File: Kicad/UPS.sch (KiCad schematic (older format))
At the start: 6 parts, among them J1 Raspberry_Pi_2_3, U1 CW2015

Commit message: Placing component
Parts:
- added D? (x4): LED, symbol Device:LED
- added SW?: SW_Push, symbol Switch:SW_Push
- added U?: ip5306, symbol ip5306:ip5306
- added U?: ETA1096, symbol eta1096:ETA1096
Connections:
- wire segments 20 -> 37
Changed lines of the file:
@@
 Text Label 6400 3650 0    50   ~ 0
 GND
+Wire Notes Line
+	750  1150 1300 1150
+Wire Notes Line
+	1300 1150 1300 2850
+Wire Notes Line
+	1300 2850 750  2850
+Wire Notes Line
+	750  2850 750  1150
+$Comp
+L eta1096:ETA1096 U?
+U 1 1 5D5AC856
+P 4000 4200
+F 0 "U?" H 3950 4225 50  0000 C CNN
+F 1 "ETA1096" H 3950 4134 50  0000 C CNN
+F 2 "" V 4350 3900 50  0001 C CNN
+F 3 "" V 4350 3900 50  0001 C CNN
+	1    4000 4200
+	1    0    0    -1
+$EndComp
+$Comp
+L ip5306:ip5306 U?
+U 1 1 5D5AA443
+P 4000 3150
+F 0 "U?" H 3950 3175 50  0000 C CNN
+F 1 "ip5306" H 3950 3084 50  0000 C CNN
+F 2 "" V 4350 2850 50  0001 C CNN
+F 3 "" V 4350 2850 50  0001 C CNN
+	1    4000 3150
+	1    0    0    -1
+$EndComp
+$Comp
+L Device:LED D?
+U 1 1 5D5ABF8A
+P 1900 3800
+F 0 "D?" V 1847 3878 50  0000 L CNN
+F 1 "LED" V 1938 3878 50  0000 L CNN
+F 2 "" H 1900 3800 50  0001 C CNN
+F 3 "~" H 1900 3800 50  0001 C CNN
+	1    1900 3800
+	0    1    1    0
+$EndComp
+$Comp
+L Device:LED D?
+U 1 1 5D5ACEC5
+P 2200 3800
+F 0 "D?" V 2239 3683 50  0000 R CNN
+F 1 "LED" V 2148 3683 50  0000 R CNN
+F 2 "" H 2200 3800 50  0001 C CNN
+F 3 "~" H 2200 3800 50  0001 C CNN
+	1    2200 3800
+	0    -1   -1   0
+$EndComp
+$Comp
+L Device:LED D?
+U 1 1 5D5ADF77
+P 2750 3800
+F 0 "D?" H 2743 4016 50  0000 C CNN
+F 1 "LED" H 2743 3925 50  0000 C CNN
+F 2 "" H 2750 3800 50  0001 C CNN
+F 3 "~" H 2750 3800 50  0001 C CNN
+	1    2750 3800
+	0    1    1    0
+$EndComp
+$Comp
+L Switch:SW_Push SW?
+U 1 1 5D5B17EF
+P 4500 3450
+F 0 "SW?" H 4500 3735 50  0000 C CNN
+F 1 "SW_Push" H 4500 3644 50  0000 C CNN
+F 2 "" H 4500 3650 50  0001 C CNN
+F 3 "~" H 4500 3650 50  0001 C CNN
+	1    4500 3450
+	1    0    0    -1
+$EndComp
+$Comp
+L Device:LED D?
+U 1 1 5D5B6623
+P 1550 3800
+F 0 "D?" V 1589 3683 50  0000 R CNN
+F 1 "LED" V 1498 3683 50  0000 R CNN
+F 2 "" H 1550 3800 50  0001 C CNN
+F 3 "~" H 1550 3800 50  0001 C CNN
+	1    1550 3800
+	0    -1   -1   0
+$EndComp
+Wire Wire Line
+	1550 3950 1900 3950
+Wire Wire Line
+	1900 3950 2200 3950
+Connection ~ 1900 3950
+Wire Wire Line
+	2200 3950 2750 3950
+Connection ~ 2200 3950
+Wire Wire Line
+	2200 3650 2750 3650
+Wire Wire Line
+	1550 3650 1550 3450
+Wire Wire Line
+	1550 3450 1900 3450
+Wire Wire Line
+	1900 3650 1900 3450
+Connection ~ 1900 3450
+Wire Wire Line
+	1900 3450 3600 3450
+Wire Wire Line
+	2750 3950 3400 3950
+Wire Wire Line
+	3400 3950 3400 3650
+Wire Wire Line
+	3400 3650 3600 3650
+Connection ~ 2750 3950
+Wire Wire Line
+	3600 3550 2750 3550
+Wire Wire Line
+	2750 3550 2750 3650
+Connection ~ 2750 3650
+Wire Wire Line
+	3600 3350 1300 3350
+Wire Wire Line
+	4300 3650 4600 3650
+Wire Wire Line
+	4600 3650 4600 3850
+Wire Wire Line
+	4300 3550 4950 3550
+Text Label 3950 3950 0    50   ~ 0
+GND
 $EndSCHEMATC

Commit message: Wiring all chip
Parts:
- added .: 1UH, symbol pspice:INDUCTOR
- added C1, C6, C?: 10µf, symbol Device:C
- added C2, C3, C4, C5, C6, C7: 22µf, symbol Device:C
- added C?: 1µf, symbol Device:C
- added C? (x2): C, symbol Device:C
- added D?: LED, symbol Device:LED
- added J?: USB_B_Micro, symbol Connector:USB_B_Micro
- added L?: INDUCTOR, symbol pspice:INDUCTOR
- added Q?: Q_PNP_BCE, symbol Device:Q_PNP_BCE
- added R1: OPTIONAL, symbol Device:R
- added R2: 100K, symbol Device:R
- added R3: 2R, symbol Device:R
- added R4: 0.5R 0603, symbol Device:R
- added R6: 43K, symbol Device:R
- added R7: 75K, symbol Device:R
- added R8, R9: 51K, symbol Device:R
- added R? (x4): R, symbol Device:R
- added Riset: ohm, symbol Device:R
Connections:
- net labels added: EN, VIN, VOUT
- wire segments 37 -> 110
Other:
- moved on the sheet: D?, SW?, U?

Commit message: Add label
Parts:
- gave numbers to parts that had none: 19
- renumbered . to .1, C6 to C1, C2 to C10, C1 to C2, C2 to C3, C1 to C4, C3 to C5, C4 to C6, C5 to C7, C7 to C8, C6 to C9, J1 to J2, R3 to R1, R4 to R10, R2 to R11, R1 to R12, R1 to R3, R8 to R6, R9 to R7, R6 to R8, R7 to R9, Riset to Riset1, U1 to U2
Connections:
- net labels added: +3.3V, +5V, NC
- wire segments 110 -> 126
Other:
- moved on the sheet: .1, C3, L1

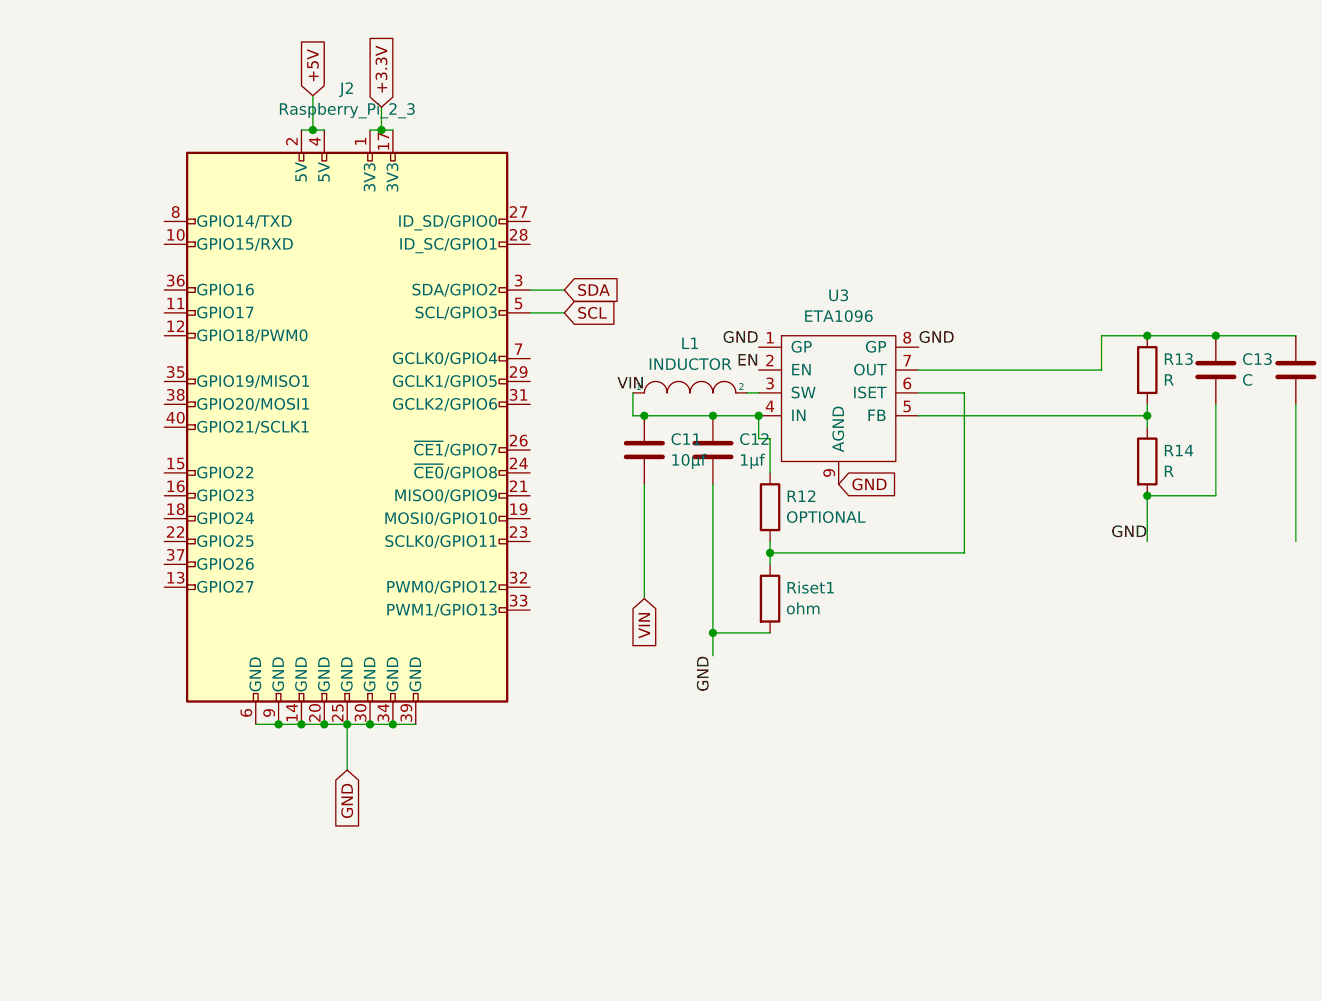
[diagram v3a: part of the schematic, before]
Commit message: Add Raspberry connector with all label marked
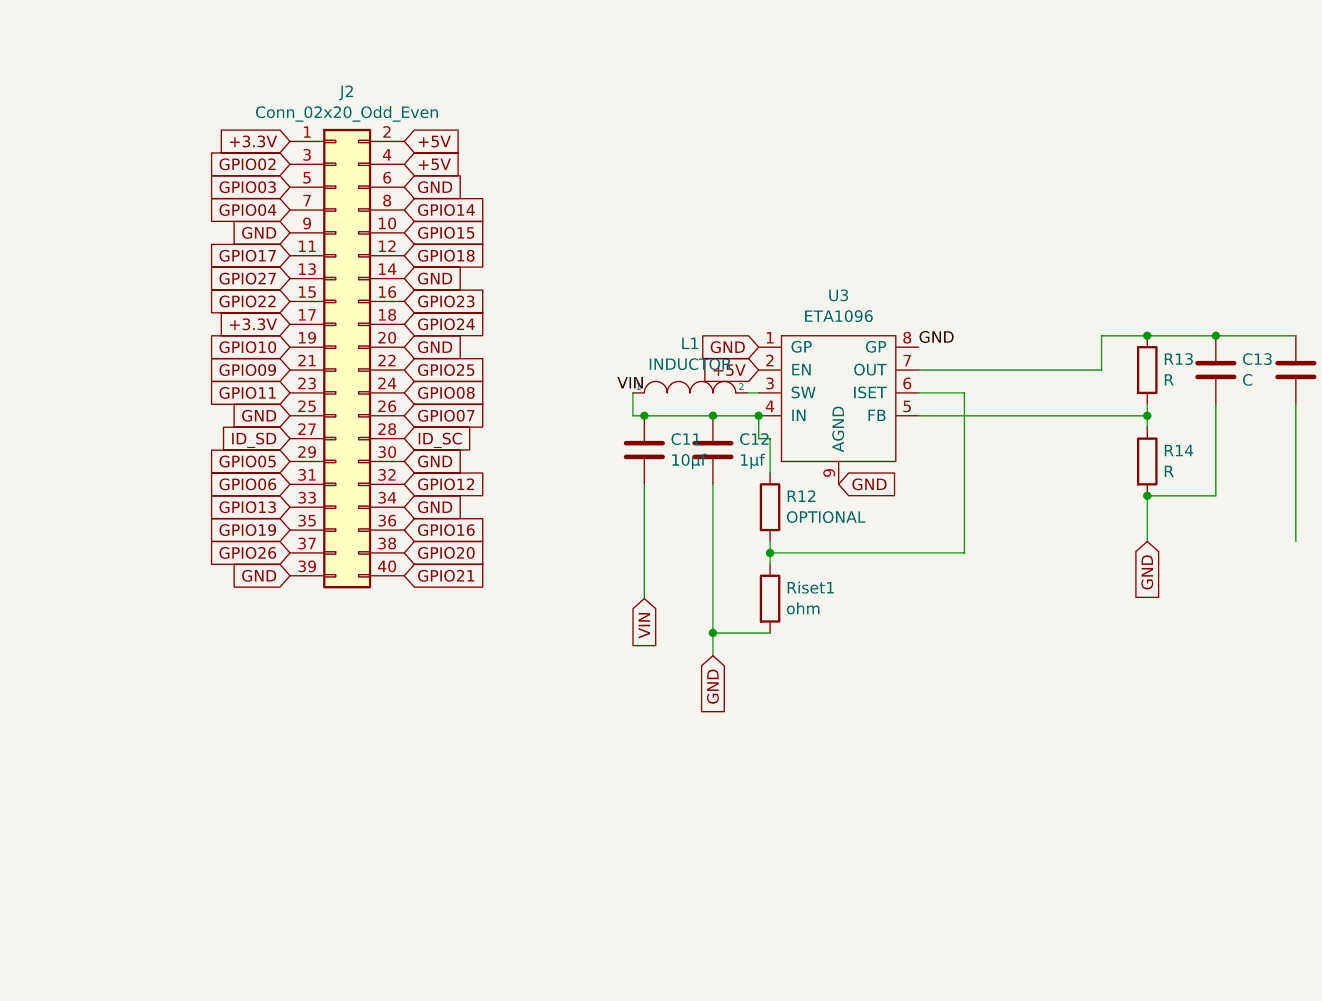
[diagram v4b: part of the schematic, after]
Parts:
- removed J2: Raspberry_Pi_2_3, symbol Connector:Raspberry_Pi_2_3
- added J2: Conn_02x20_Odd_Even, symbol Connector_Generic:Conn_02x20_Odd_Even
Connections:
- net EN is gone; now on net +5V: U3.2 (EN)
- net +3.3V: now also J2.1 (Pin_1), J2.17 (Pin_17)
- net +5V: now also J2.2 (Pin_2), J2.4 (Pin_4)
- net GND: now also J2.14 (Pin_14), J2.20 (Pin_20), J2.25 (Pin_25), J2.30 (Pin_30), J2.34 (Pin_34), J2.39 (Pin_39), J2.6 (Pin_6), J2.9 (Pin_9)
- new net GPIO02: J2.3 (Pin_3)
- new net GPIO03: J2.5 (Pin_5)
- new net GPIO04: J2.7 (Pin_7)
- new net GPIO05: J2.29 (Pin_29)
- new net GPIO06: J2.31 (Pin_31)
- new net GPIO07: J2.26 (Pin_26)
- new net GPIO08: J2.24 (Pin_24)
- new net GPIO09: J2.21 (Pin_21)
- new net GPIO10: J2.19 (Pin_19)
- new net GPIO11: J2.23 (Pin_23)
- new net GPIO12: J2.32 (Pin_32)
- new net GPIO13: J2.33 (Pin_33)
- new net GPIO14: J2.8 (Pin_8)
- new net GPIO15: J2.10 (Pin_10)
- new net GPIO16: J2.36 (Pin_36)
- new net GPIO17: J2.11 (Pin_11)
- new net GPIO18: J2.12 (Pin_12)
- new net GPIO19: J2.35 (Pin_35)
- new net GPIO20: J2.38 (Pin_38)
- new net GPIO21: J2.40 (Pin_40)
- new net GPIO22: J2.15 (Pin_15)
- new net GPIO23: J2.16 (Pin_16)
- new net GPIO24: J2.18 (Pin_18)
- new net GPIO25: J2.22 (Pin_22)
- new net GPIO26: J2.37 (Pin_37)
- new net GPIO27: J2.13 (Pin_13)
- new net ID_SC: J2.28 (Pin_28)
- new net ID_SD: J2.27 (Pin_27)
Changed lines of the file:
@@
 	2450 1450 1250 1450
 Connection ~ 2450 1450
-$Comp
-L Connector:Raspberry_Pi_2_3 J2
-U 1 1 5D5AFDE6
-P 6400 2150
-F 0 "J2" H 6400 3631 50  0000 C CNN
-F 1 "Raspberry_Pi_2_3" H 6400 3540 50  0000 C CNN
-F 2 "" H 6400 2150 50  0001 C CNN
-F 3 "https://www.raspberrypi.org/documentation/hardware/raspberrypi/schematics/rpi_SCH_3bplus_1p0_reduced.pdf" H 6400 2150 50  0001 C CNN
-	1    6400 2150
-	1    0    0    -1
-$EndComp
-Wire Wire Line
-	6000 3450 6100 3450
-Connection ~ 6100 3450
-Wire Wire Line
-	6100 3450 6200 3450
-Connection ~ 6200 3450
-Wire Wire Line
-	6200 3450 6300 3450
-Connection ~ 6300 3450
-Wire Wire Line
-	6300 3450 6400 3450
-Connection ~ 6400 3450
-Wire Wire Line
-	6400 3450 6500 3450
-Connection ~ 6500 3450
-Wire Wire Line
-	6500 3450 6600 3450
-Connection ~ 6600 3450
-Wire Wire Line
-	6600 3450 6700 3450
-Wire Wire Line
-	6400 3450 6400 3650
 Wire Notes Line
 	750  1150 1300 1150
@@
 Text Label 8900 1800 0    50   ~ 0
 GND
-Text Label 8200 1800 2    50   ~ 0
-GND
-Text Label 8200 1900 2    50   ~ 0
-EN
 $Comp
 L pspice:INDUCTOR L1
@@
 Wire Wire Line
 	9100 2700 9100 2000
-Text Label 8000 3150 3    50   ~ 0
-GND
 Wire Wire Line
 	8000 3050 8000 3150
@@
 Wire Wire Line
 	10550 2050 10550 2650
-Text Label 9900 2650 2    50   ~ 0
-GND
 Wire Wire Line
 	8900 2100 9900 2100
@@
 Text GLabel 1050 5250 2    50   Input ~ 0
 NC
-Text GLabel 6550 750  1    50   Input ~ 0
-+3.3V
-Text GLabel 6250 700  1    50   Input ~ 0
-+5V
-Wire Wire Line
-	6500 850  6550 850
-Wire Wire Line
-	6200 850  6250 850
-Wire Wire Line
-	6250 850  6250 700
-Connection ~ 6250 850
-Wire Wire Line
-	6250 850  6300 850
-Wire Wire Line
-	6550 850  6550 750
-Connection ~ 6550 850
-Wire Wire Line
-	6550 850  6600 850
 Wire Wire Line
 	1250 2550 2450 2550
@@
 Wire Wire Line
 	4450 2050 4300 2050
-Text GLabel 7350 1550 2    50   Input ~ 0
-SDA
-Text GLabel 7350 1650 2    50   Input ~ 0
-SCL
-Wire Wire Line
-	7350 1550 7200 1550
-Wire Wire Line
-	7350 1650 7200 1650
-Text GLabel 6400 3650 3    50   Input ~ 0
-GND
 Text GLabel 5900 6950 0    50   Input ~ 0
 VOUT
@@
 Wire Wire Line
 	6000 6950 6000 7000
+$Comp
+L Connector_Generic:Conn_02x20_Odd_Even J2
+U 1 1 5D5EA04E
+P 6350 1800
+F 0 "J2" H 6400 2917 50  0000 C CNN
+F 1 "Conn_02x20_Odd_Even" H 6400 2826 50  0000 C CNN
+F 2 "" H 6350 1800 50  0001 C CNN
+F 3 "~" H 6350 1800 50  0001 C CNN
+	1    6350 1800
+	1    0    0    -1
+$EndComp
+Text GLabel 6150 900  0    50   Input ~ 0
++3.3V
+Text GLabel 6650 900  2    50   Input ~ 0
++5V
+Text GLabel 6650 1000 2    50   Input ~ 0
++5V
+Text GLabel 6650 1100 2    50   Input ~ 0
+GND
+Text GLabel 6650 1200 2    50   Input ~ 0
+GPIO14
+Text GLabel 6650 1300 2    50   Input ~ 0
+GPIO15
+Text GLabel 6650 1400 2    50   Input ~ 0
+GPIO18
+Text GLabel 6650 1500 2    50   Input ~ 0
+GND
+Text GLabel 6650 1600 2    50   Input ~ 0
+GPIO23
+Text GLabel 6650 1700 2    50   Input ~ 0
+GPIO24
+Text GLabel 6650 1800 2    50   Input ~ 0
+GND
+Text GLabel 6650 1900 2    50   Input ~ 0
+GPIO25
+Text GLabel 6650 2000 2    50   Input ~ 0
+GPIO08
+Text GLabel 6650 2100 2    50   Input ~ 0
+GPIO07
+Text GLabel 6650 2200 2    50   Input ~ 0
+ID_SC
+Text GLabel 6650 2300 2    50   Input ~ 0
+GND
+Text GLabel 6650 2400 2    50   Input ~ 0
+GPIO12
+Text GLabel 6650 2500 2    50   Input ~ 0
+GND
+Text GLabel 6650 2600 2    50   Input ~ 0
+GPIO16
+Text GLabel 6650 2700 2    50   Input ~ 0
+GPIO20
+Text GLabel 6650 2800 2    50   Input ~ 0
+GPIO21
+Text GLabel 6150 2800 0    50   Input ~ 0
+GND
+Text GLabel 6150 2700 0    50   Input ~ 0
+GPIO26
+Text GLabel 6150 2600 0    50   Input ~ 0
+GPIO19
+Text GLabel 6150 2500 0    50   Input ~ 0
+GPIO13
+Text GLabel 6150 2400 0    50   Input ~ 0
+GPIO06
+Text GLabel 6150 2300 0    50   Input ~ 0
+GPIO05
+Text GLabel 6150 2200 0    50   Input ~ 0
+ID_SD
+Text GLabel 6150 2100 0    50   Input ~ 0
+GND
+Text GLabel 6150 2000 0    50   Input ~ 0
+GPIO11
+Text GLabel 6150 1900 0    50   Input ~ 0
+GPIO09
+Text GLabel 6150 1800 0    50   Input ~ 0
+GPIO10
+Text GLabel 6150 1700 0    50   Input ~ 0
++3.3V
+Text GLabel 6150 1600 0    50   Input ~ 0
+GPIO22
+Text GLabel 6150 1500 0    50   Input ~ 0
+GPIO27
+Text GLabel 6150 1400 0    50   Input ~ 0
+GPIO17
+Text GLabel 6150 1300 0    50   Input ~ 0
+GND
+Text GLabel 6150 1200 0    50   Input ~ 0
+GPIO04
+Text GLabel 6150 1100 0    50   Input ~ 0
+GPIO03
+Text GLabel 6150 1000 0    50   Input ~ 0
+GPIO02
+Text GLabel 8000 3150 3    50   Input ~ 0
+GND
+Text GLabel 9900 2650 3    50   Input ~ 0
+GND
+Text GLabel 8200 1800 0    50   Input ~ 0
+GND
+Text GLabel 8200 1900 0    50   Input ~ 0
++5V
 $EndSCHEMATC

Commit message: Minor change
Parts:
- added J10: GET_UP_SERVO_RIGHT, symbol Connector:Conn_01x03_Female
- added J11: SPI, symbol Connector:Conn_01x05_Female
- added J12: I2C, symbol Connector:Conn_01x04_Female
- added J3: X_HEAD_PAN, symbol Connector:Conn_01x03_Female
- added J4: Y_HEAD_PAN, symbol Connector:Conn_01x03_Female
- added J5: X_CLAW, symbol Connector:Conn_01x03_Female
- added J6: Y_CLAW, symbol Connector:Conn_01x03_Female
- added J7: MOTOR_LEFT, symbol Connector:Conn_01x03_Female
- added J8: MOTOR_RIGHT, symbol Connector:Conn_01x03_Female
- added J9: GET_UP_SERVO_LEFT, symbol Connector:Conn_01x03_Female
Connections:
- net SCL is gone; now on net GPIO03: U2.7 (SCL)
- net SDA is gone; now on net GPIO02: U2.8 (SDA)
- net +3.3V: now also J11.1 (Pin_1), J12.3 (Pin_3)
- net +5V: now also J10.2 (Pin_2), J3.2 (Pin_2), J4.2 (Pin_2), J5.2 (Pin_2), J6.2 (Pin_2), J7.2 (Pin_2), J8.2 (Pin_2), J9.2 (Pin_2)
- net BATT+: now also .1.1; no longer .1.2
- net GND: now also U2.4 (GND), J10.3 (Pin_3), J11.5 (Pin_5), J12.4 (Pin_4), J3.3 (Pin_3), J4.3 (Pin_3), J5.3 (Pin_3), J6.3 (Pin_3), J7.3 (Pin_3), J8.3 (Pin_3), J9.3 (Pin_3)
- net GPIO02: now also J12.1 (Pin_1)
- net GPIO03: now also J12.2 (Pin_2)
- net GPIO05: now also J3.1 (Pin_1)
- net GPIO06: now also J4.1 (Pin_1)
- net GPIO07: now also J5.1 (Pin_1)
- net GPIO08: now also J6.1 (Pin_1)
- net GPIO09: now also J11.2 (Pin_2)
- net GPIO10: now also J11.3 (Pin_3)
- net GPIO11: now also J11.4 (Pin_4)
- net GPIO12: now also J9.1 (Pin_1)
- net GPIO13: now also J10.1 (Pin_1)
- net GPIO26: now also J7.1 (Pin_1)
- net GPIO27: now also J8.1 (Pin_1)
- net VIN: now also C11.1, C12.1, L1.2, R12.1, U3.4 (IN)
- net at U1.7 (SW): now also .1.2; no longer .1.1
- net at U3.3 (SW): now also L1.1; no longer L1.2
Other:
- moved on the sheet: .1, L1
